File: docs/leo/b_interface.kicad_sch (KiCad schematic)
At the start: 8 parts, among them IC37 74LS245, IC38 74LS244, IC39 74LS374, IC40 74LS245, IC46 74LS161, IC47 GAL16V8, IC48 74LS374, IC49 74LS244

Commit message: Add more b board logic
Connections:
- net ~{EEPROM_REQ}: now reaches IC47.15 (IO5)
- net EEPROM_REQ: now reaches IC47.16 (IO4)
- net IC27_115: now reaches IC48.1 (OE)
- net IC27_115: now also IC39.1 (OE)
- net VRAM_CPU_WINDOW: now reaches IC39.11 (Cp), IC46.12 (Q2), IC48.11 (Cp)
- net VCC: now reaches IC46.1 (~{MR})
- net VCC: now also IC46.10 (CET), IC46.16 (VCC), IC46.3 (D0), IC46.5 (D2), IC46.7 (CEP)
- net CLK_PIXEL: now reaches IC46.2 (CP)
- net GND: now reaches IC46.4 (D1)
- net GND: now also IC46.6 (D3), IC46.8 (GND)
- net H_PULSE: now reaches IC46.9 (~{PE})
- net BUF_EN renamed ~{LS245_EN}
- no-connect marks 0 -> 4

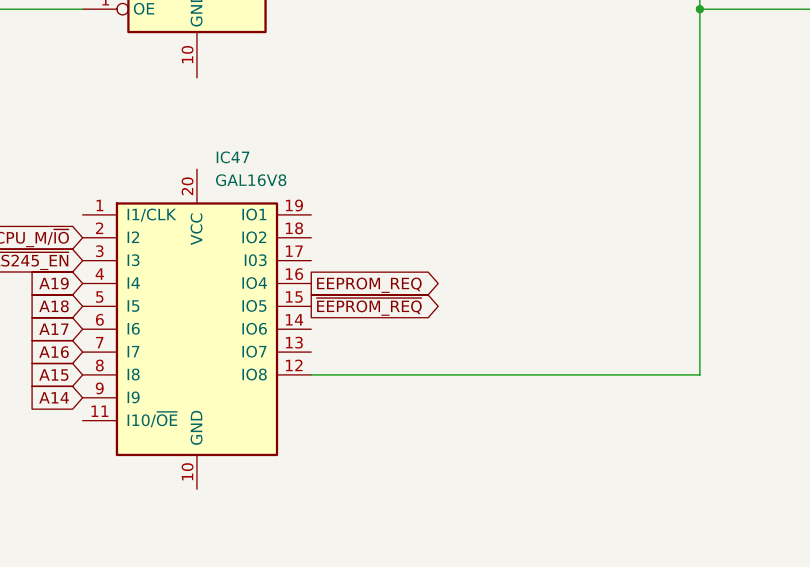
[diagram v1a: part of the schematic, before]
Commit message: Decode M92-B-7H-D PAL
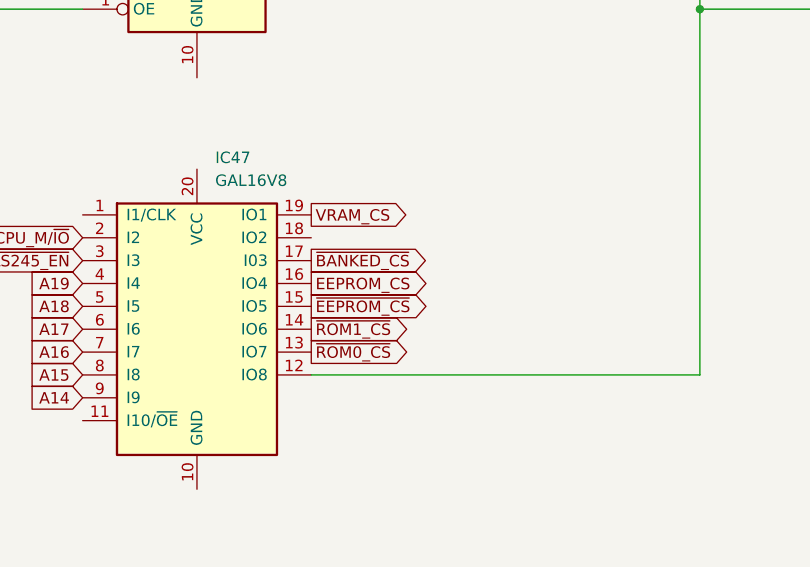
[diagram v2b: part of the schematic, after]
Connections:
- net ~{ROM0_CS}: now reaches IC47.13 (IO7)
- net ~{ROM1_CS}: now reaches IC47.14 (IO6)
- net ~{BANKED_CS}: now reaches IC47.17 (I03)
- net VRAM_CS: now reaches IC47.19 (IO1)
- net EEPROM_REQ renamed EEPROM_CS
- net ~{EEPROM_REQ} renamed ~{EEPROM_CS}
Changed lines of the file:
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@@
+    )
+  )
+  (global_label "~{ROM0_CS}" (shape output) (at 156.21 147.32 0) (fields_autoplaced)
+    (effects (font (size 1.27 1.27)) (justify left))
+    (property "Intersheet References" "${INTERSHEET_REFS}" (id 0) (at 167.3317 147.2406 0)
+      (effects (font (size 1.27 1.27)) (justify left) hide)
     )
   )
@@
     )
   )
-  (global_label "~{EEPROM_REQ}" (shape output) (at 156.21 142.24 0) (fields_autoplaced)
-    (effects (font (size 1.27 1.27)) (justify left))
-    (property "Intersheet References" "${INTERSHEET_REFS}" (id 0) (at 170.9602 142.1606 0)
+  (global_label "~{EEPROM_CS}" (shape output) (at 156.21 142.24 0) (fields_autoplaced)
+    (effects (font (size 1.27 1.27)) (justify left))
+    (property "Intersheet References" "${INTERSHEET_REFS}" (id 0) (at 169.6902 142.1606 0)
       (effects (font (size 1.27 1.27)) (justify left) hide)
     )
@@
     )
   )
+  (global_label "~{BANKED_CS}" (shape output) (at 156.21 137.16 0) (fields_autoplaced)
+    (effects (font (size 1.27 1.27)) (justify left))
+    (property "Intersheet References" "${INTERSHEET_REFS}" (id 0) (at 169.4483 137.0806 0)
+      (effects (font (size 1.27 1.27)) (justify left) hide)
+    )
+  )
   (global_label "CPU_D1" (shape input) (at 156.21 46.99 0) (fields_autoplaced)
     (effects (font (size 1.27 1.27)) (justify left))
@@
     )
   )
+  (global_label "~{ROM1_CS}" (shape output) (at 156.21 144.78 0) (fields_autoplaced)
+    (effects (font (size 1.27 1.27)) (justify left))
+    (property "Intersheet References" "${INTERSHEET_REFS}" (id 0) (at 167.3317 144.7006 0)
+      (effects (font (size 1.27 1.27)) (justify left) hide)
+    )
+  )
   (global_label "VRAM_D11" (shape input) (at 71.12 95.25 0) (fields_autoplaced)
     (effects (font (size 1.27 1.27)) (justify left))
@@
     )
   )
-  (global_label "EEPROM_REQ" (shape output) (at 156.21 139.7 0) (fields_autoplaced)
-    (effects (font (size 1.27 1.27)) (justify left))
-    (property "Intersheet References" "${INTERSHEET_REFS}" (id 0) (at 170.9602 139.6206 0)
-      (effects (font (size 1.27 1.27)) (justify left) hide)
-    )
+  (global_label "EEPROM_CS" (shape output) (at 156.21 139.7 0) (fields_autoplaced)
+    (effects (font (size 1.27 1.27)) (justify left))
+    (property "Intersheet References" "${INTERSHEET_REFS}" (id 0) (at 169.6902 139.6206 0)
+      (effects (font (size 1.27 1.27)) (justify left) hide)
+    )
+  )
+  (global_label "VRAM_CS" (shape output) (at 156.21 132.08 0) (fields_autoplaced)
+    (effects (font (size 1.27 1.27)) (justify left))
+    (property "Intersheet References" "${INTERSHEET_REFS}" (id 0) (at 166.9688 132.0006 0)
+      (effects (font (size 1.27 1.27)) (justify left) hide)
+    )

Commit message: Rough out 08J27504
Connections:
- net IC27_115 renamed ~{VRAM_RD}
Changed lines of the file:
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@@
     )
   )
-  (global_label "IC27_115" (shape input) (at 99.06 57.15 180) (fields_autoplaced)
+  (global_label "~{VRAM_RD}" (shape input) (at 99.06 57.15 180) (fields_autoplaced)
     (effects (font (size 1.27 1.27)) (justify right))
-    (property "Intersheet References" "${INTERSHEET_REFS}" (id 0) (at 87.7569 57.0706 0)
+    (property "Intersheet References" "${INTERSHEET_REFS}" (id 0) (at 88.2407 57.0706 0)
       (effects (font (size 1.27 1.27)) (justify right) hide)
     )
